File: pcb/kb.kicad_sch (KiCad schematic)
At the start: 131 parts, among them J1 S2B-PH-SM4-TB, SW0 SW_SPDT, SW1 Gateron_LP_2.0, SW10 Gateron_LP_2.0, SW11 Gateron_LP_2.0, SW12 Gateron_LP_2.0, SW13 Gateron_LP_2.0, SW14 Gateron_LP_2.0, SW15 Gateron_LP_2.0, SW16 Gateron_LP_2.0, SW17 Gateron_LP_2.0, SW18 Gateron_LP_2.0, SW19 Gateron_LP_2.0, SW2 Gateron_LP_2.0, SW20 Gateron_LP_2.0, SW21 Gateron_LP_2.0, SW22 Gateron_LP_2.0, SW23 Gateron_LP_2.0, SW24 Gateron_LP_2.0, SW25 Gateron_LP_2.0, SW26 Gateron_LP_2.0, SW27 Gateron_LP_2.0, SW28 Gateron_LP_2.0, SW29 Gateron_LP_2.0, SW3 Gateron_LP_2.0, SW30 Gateron_LP_2.0, SW31 Gateron_LP_2.0, SW32 Gateron_LP_2.0, SW33 Gateron_LP_2.0, SW34 Gateron_LP_2.0, SW35 Gateron_LP_2.0, SW36 Gateron_LP_2.0, SW37 Gateron_LP_2.0, SW38 Gateron_LP_2.0, SW39 Gateron_LP_2.0, SW4 Gateron_LP_2.0, SW40 Gateron_LP_2.0, SW41 Gateron_LP_2.0, SW42 Gateron_LP_2.0, SW43 Gateron_LP_2.0, SW44 Gateron_LP_2.0, SW45 Gateron_LP_2.0, SW46 Gateron_LP_2.0, SW47 Gateron_LP_2.0, SW48 Gateron_LP_2.0, SW49 Gateron_LP_2.0, SW5 Gateron_LP_2.0, SW50 Gateron_LP_2.0, SW51 Gateron_LP_2.0, SW52 Gateron_LP_2.0, SW53 Gateron_LP_2.0, SW54 Gateron_LP_2.0, SW55 Gateron_LP_2.0, SW56 Gateron_LP_2.0, SW57 Gateron_LP_2.0, SW58 Gateron_LP_2.0, SW59 Gateron_LP_2.0, SW6 Gateron_LP_2.0, SW60 Gateron_LP_2.0, SW61 Gateron_LP_2.0, SW62 Gateron_LP_2.0, SW63 Gateron_LP_2.0, SW64 Gateron_LP_2.0, SW7 Gateron_LP_2.0, SW8 Gateron_LP_2.0, SW9 Gateron_LP_2.0, U1 SuperMini nRF52840

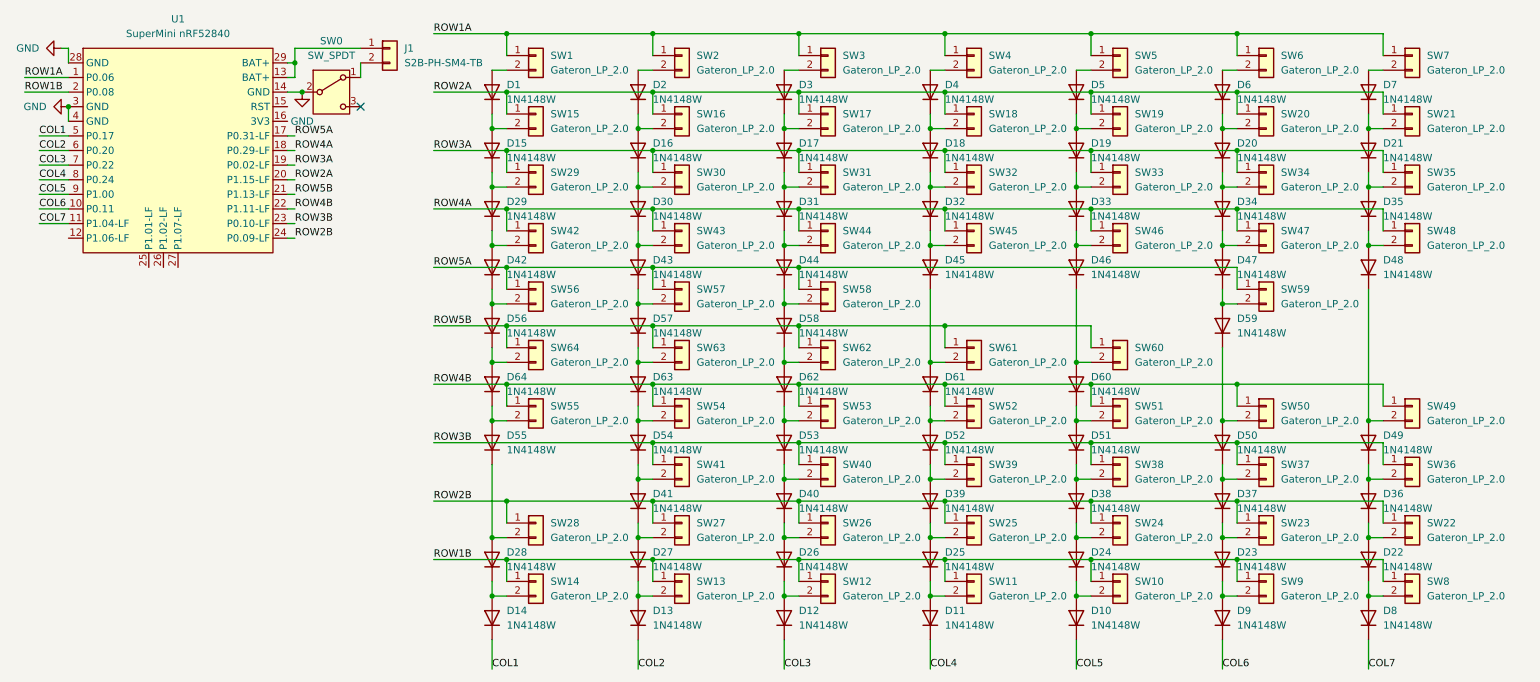
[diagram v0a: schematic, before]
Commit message: parallel diodes
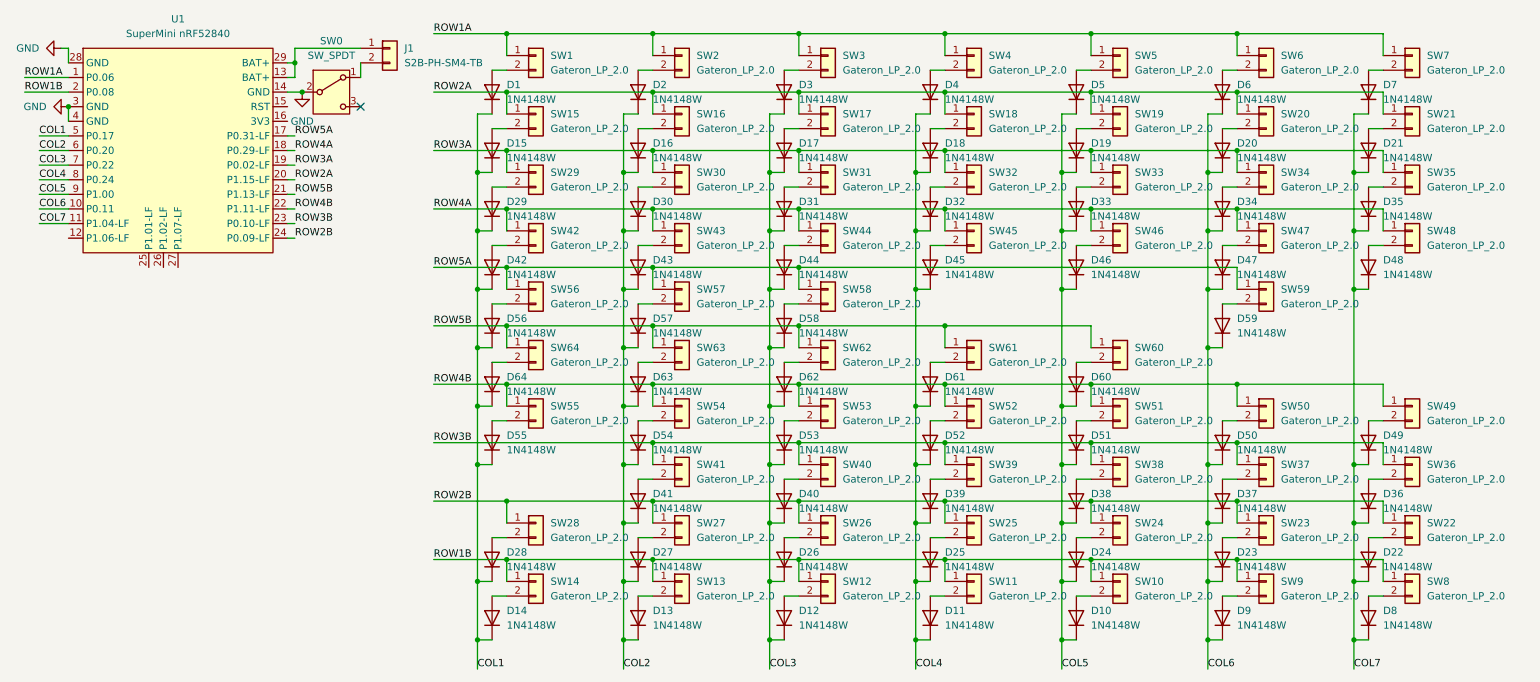
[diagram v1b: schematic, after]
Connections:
- net COL1: now also D1.1 (K), D15.1 (K), D28.1 (K), D29.1 (K), D42.1 (K), D55.1 (K), D56.1 (K), D64.1 (K)
- net COL2: now also D16.1 (K), D2.1 (K), D27.1 (K), D30.1 (K), D41.1 (K), D43.1 (K), D54.1 (K), D57.1 (K), D63.1 (K)
- net COL3: now also D17.1 (K), D26.1 (K), D3.1 (K), D31.1 (K), D40.1 (K), D44.1 (K), D53.1 (K), D58.1 (K), D62.1 (K)
- net COL4: now also D18.1 (K), D25.1 (K), D32.1 (K), D39.1 (K), D4.1 (K), D45.1 (K), D52.1 (K), D61.1 (K)
- net COL5: now also D19.1 (K), D24.1 (K), D33.1 (K), D38.1 (K), D46.1 (K), D5.1 (K), D51.1 (K), D60.1 (K)
- net COL6: now also D20.1 (K), D23.1 (K), D34.1 (K), D37.1 (K), D47.1 (K), D50.1 (K), D59.1 (K), D6.1 (K)
- net COL7: now also D21.1 (K), D22.1 (K), D35.1 (K), D36.1 (K), D48.1 (K), D49.1 (K), D7.1 (K)
- net at D64.2 (A), SW64.2 (Pin_2): no longer D56.1 (K)
- net at D46.2 (A), SW46.2 (Pin_2): no longer D33.1 (K)
- net at D22.2 (A), SW22.2 (Pin_2): no longer D36.1 (K)
- net at D45.2 (A), SW45.2 (Pin_2): no longer D32.1 (K)
- net at D36.2 (A), SW36.2 (Pin_2): no longer D49.1 (K)
- net at D39.2 (A), SW39.2 (Pin_2): no longer D52.1 (K)
- net at D21.2 (A), SW21.2 (Pin_2): no longer D7.1 (K)
- net at D29.2 (A), SW29.2 (Pin_2): no longer D15.1 (K)
- net at D18.2 (A), SW18.2 (Pin_2): no longer D4.1 (K)
- net at D11.2 (A), SW11.2 (Pin_2): no longer D25.1 (K)
- net at D33.2 (A), SW33.2 (Pin_2): no longer D19.1 (K)
- net at D19.2 (A), SW19.2 (Pin_2): no longer D5.1 (K)
- net at D25.2 (A), SW25.2 (Pin_2): no longer D39.1 (K)
- net at D8.2 (A), SW8.2 (Pin_2): no longer D22.1 (K)
- net at D12.2 (A), SW12.2 (Pin_2): no longer D26.1 (K)
- net at D34.2 (A), SW34.2 (Pin_2): no longer D20.1 (K)
- net at D20.2 (A), SW20.2 (Pin_2): no longer D6.1 (K)
- net at D15.2 (A), SW15.2 (Pin_2): no longer D1.1 (K)
- net at D37.2 (A), SW37.2 (Pin_2): no longer D50.1 (K)
- net at D50.2 (A), SW50.2 (Pin_2): no longer D59.1 (K)
- net at D40.2 (A), SW40.2 (Pin_2): no longer D53.1 (K)
- net at D43.2 (A), SW43.2 (Pin_2): no longer D30.1 (K)
- net at D52.2 (A), SW52.2 (Pin_2): no longer D61.1 (K)
- net at D57.2 (A), SW57.2 (Pin_2): no longer D43.1 (K)
- net at D17.2 (A), SW17.2 (Pin_2): no longer D3.1 (K)
- net at D51.2 (A), SW51.2 (Pin_2): no longer D60.1 (K)
- net at D60.2 (A), SW60.2 (Pin_2): no longer D46.1 (K)
- net at D30.2 (A), SW30.2 (Pin_2): no longer D16.1 (K)
- net at D9.2 (A), SW9.2 (Pin_2): no longer D23.1 (K)
- net at D26.2 (A), SW26.2 (Pin_2): no longer D40.1 (K)
- net at D61.2 (A), SW61.2 (Pin_2): no longer D45.1 (K)
- net at D14.2 (A), SW14.2 (Pin_2): no longer D28.1 (K)
- net at D35.2 (A), SW35.2 (Pin_2): no longer D21.1 (K)
- net at D31.2 (A), SW31.2 (Pin_2): no longer D17.1 (K)
- net at D32.2 (A), SW32.2 (Pin_2): no longer D18.1 (K)
- net at D42.2 (A), SW42.2 (Pin_2): no longer D29.1 (K)
- net at D16.2 (A), SW16.2 (Pin_2): no longer D2.1 (K)
- net at D49.2 (A), SW49.2 (Pin_2): no longer D48.1 (K)
- net at D53.2 (A), SW53.2 (Pin_2): no longer D62.1 (K)
- net at D62.2 (A), SW62.2 (Pin_2): no longer D58.1 (K)
- net at D23.2 (A), SW23.2 (Pin_2): no longer D37.1 (K)
- net at D48.2 (A), SW48.2 (Pin_2): no longer D35.1 (K)
- net at D63.2 (A), SW63.2 (Pin_2): no longer D57.1 (K)
- net at D27.2 (A), SW27.2 (Pin_2): no longer D41.1 (K)
- net at D41.2 (A), SW41.2 (Pin_2): no longer D54.1 (K)
- net at D58.2 (A), SW58.2 (Pin_2): no longer D44.1 (K)
- net at D44.2 (A), SW44.2 (Pin_2): no longer D31.1 (K)
- net at D38.2 (A), SW38.2 (Pin_2): no longer D51.1 (K)
- net at D54.2 (A), SW54.2 (Pin_2): no longer D63.1 (K)
- net at D28.2 (A), SW28.2 (Pin_2): no longer D55.1 (K)
- net at D56.2 (A), SW56.2 (Pin_2): no longer D42.1 (K)
- net at D55.2 (A), SW55.2 (Pin_2): no longer D64.1 (K)
- net at D10.2 (A), SW10.2 (Pin_2): no longer D24.1 (K)
- net at D24.2 (A), SW24.2 (Pin_2): no longer D38.1 (K)
- net at D13.2 (A), SW13.2 (Pin_2): no longer D27.1 (K)
- net at D59.2 (A), SW59.2 (Pin_2): no longer D47.1 (K)
- net at D47.2 (A), SW47.2 (Pin_2): no longer D34.1 (K)
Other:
- title: (none) -> KB60

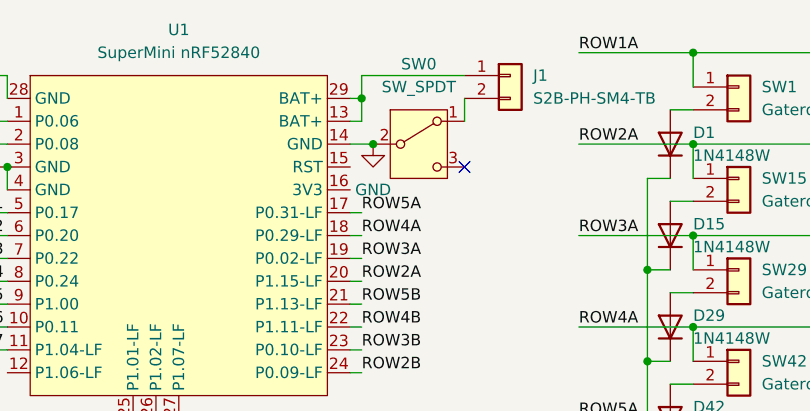
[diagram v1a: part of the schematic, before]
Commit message: fix all known issues with v1.0 pcb
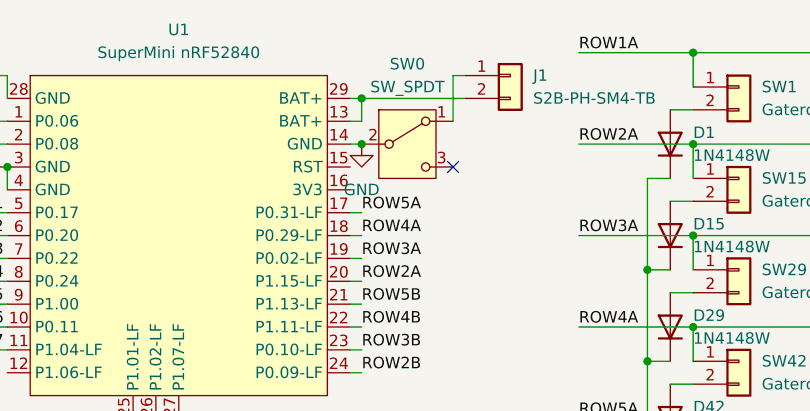
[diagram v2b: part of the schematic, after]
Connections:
- net at U1.13 (BAT+), U1.29 (BAT+): now also J1.2 (Pin_2); no longer J1.1 (Pin_1)
- net at SW0.1 (A): now also J1.1 (Pin_1); no longer J1.2 (Pin_2)
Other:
- moved on the sheet: SW0
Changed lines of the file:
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@@
 	)
 	(junction
+		(at 64.77 26.67)
+		(diameter 0)
+		(color 0 0 0 0)
+	)
+	(junction
 		(at 127 82.55)
 		(diameter 0)
@@
 	)
 	(junction
+		(at 64.77 31.75)
+		(diameter 0)
+		(color 0 0 0 0)
+	)
+	(junction
 		(at 96.52 127)
 		(diameter 0)
@@
 	)
 	(junction
-		(at 66.04 31.75)
-		(diameter 0)
-		(color 0 0 0 0)
-	)
-	(junction
 		(at 177.8 31.75)
 		(diameter 0)
@@
 	)
 	(junction
-		(at 64.77 26.67)
-		(diameter 0)
-		(color 0 0 0 0)
-	)
-	(junction
 		(at 177.8 102.87)
 		(diameter 0)
@@
 	)
 	(no_connect
-		(at 76.2 34.29)
+		(at 74.93 34.29)
 	)
 	(wire
@@
 	(wire
 		(pts
-			(xy 76.2 26.67) (xy 76.2 29.21)
-		)
-		(stroke
-			(width 0)
-			(type default)
-		)
-	)
-	(wire
-		(pts
 			(xy 175.26 119.38) (xy 177.8 119.38)
 		)
@@
 	(wire
 		(pts
+			(xy 74.93 24.13) (xy 74.93 29.21)
+		)
+		(stroke
+			(width 0)
+			(type default)
+		)
+	)
+	(wire
+		(pts
 			(xy 127 52.07) (xy 152.4 52.07)
 		)
@@
 	(wire
 		(pts
+			(xy 64.77 26.67) (xy 76.2 26.67)
+		)
+		(stroke
+			(width 0)
+			(type default)
+		)
+	)
+	(wire
+		(pts
 			(xy 121.92 76.2) (xy 121.92 86.36)
 		)
@@
 	(wire
 		(pts
-			(xy 64.77 24.13) (xy 64.77 26.67)
-		)
-		(stroke
-			(width 0)
-			(type default)
-		)
-	)
-	(wire
-		(pts
 			(xy 96.52 127) (xy 96.52 132.08)
 		)
@@
 	(wire
 		(pts
+			(xy 76.2 24.13) (xy 74.93 24.13)
+		)
+		(stroke
+			(width 0)
+			(type default)
+		)
+	)
+	(wire
+		(pts
 			(xy 175.26 99.06) (xy 177.8 99.06)
 		)
@@
 	(wire
 		(pts
-			(xy 64.77 24.13) (xy 76.2 24.13)
-		)
-		(stroke
-			(width 0)
-			(type default)
-		)
-	)
-	(wire
-		(pts
 			(xy 175.26 88.9) (xy 177.8 88.9)
 		)
@@
 	(wire
 		(pts
-			(xy 63.5 31.75) (xy 66.04 31.75)
+			(xy 63.5 31.75) (xy 64.77 31.75)
 		)
 		(stroke
@@
 	(symbol
 		(lib_id "power:GND")
-		(at 66.04 31.75 0)
+		(at 64.77 31.75 0)
 		(unit 1)
 		(exclude_from_sim no)
@@
 		(fields_autoplaced yes)
 		(property "Reference" "#PWR01"
-			(at 66.04 38.1 0)
+			(at 64.77 38.1 0)
 			(effects
 				(font
@@
 		)
 		(property "Value" "GND"
-			(at 66.04 36.83 0)
+			(at 64.77 36.83 0)
 			(effects
 				(font
@@
 		)
 		(property "Footprint" ""
-			(at 66.04 31.75 0)
+			(at 64.77 31.75 0)
 			(effects
 				(font
@@
 		)
 		(property "Datasheet" ""
-			(at 66.04 31.75 0)
+			(at 64.77 31.75 0)
 			(effects
 				(font
@@
 		)
 		(property "Description" "Power symbol creates a global label with name \"GND\" , ground"
-			(at 66.04 31.75 0)
+			(at 64.77 31.75 0)
 			(effects
 				(font
@@
 	(symbol
 		(lib_id "Switch:SW_SPDT")
-		(at 71.12 31.75 0)
+		(at 69.85 31.75 0)
 		(unit 1)
 		(exclude_from_sim no)
@@
 		(fields_autoplaced yes)
 		(property "Reference" "SW0"
-			(at 71.12 22.86 0)
+			(at 69.85 22.86 0)
 			(effects
 				(font
@@
 		)
 		(property "Value" "SW_SPDT"
-			(at 71.12 25.4 0)
+			(at 69.85 25.4 0)
 			(effects
 				(font
@@
 		)
 		(property "Footprint" "Button_Switch_SMD:SW_SPDT_CK_JS102011SAQN"
-			(at 71.12 31.75 0)
+			(at 69.85 31.75 0)
 			(effects
 				(font
@@
 		)
 		(property "Datasheet" "~"
-			(at 71.12 39.37 0)
+			(at 69.85 39.37 0)
 			(effects
 				(font
@@
 		)
 		(property "Description" "Switch, single pole double throw"
-			(at 71.12 31.75 0)
+			(at 69.85 31.75 0)
 			(effects
 				(font

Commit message: update footprints + bom
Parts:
- SW0: footprint Button_Switch_SMD:SW_SPDT_CK_JS102011SAQN -> alpsalpine:SW_SSSS811101
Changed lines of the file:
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@@
 	(title_block
 		(title "KB60")
-		(date "2025-12-26")
+		(date "2025-12-27")
 		(rev "V1.1")
 	)
@@
 			)
 		)
-		(property "Footprint" "Button_Switch_SMD:SW_SPDT_CK_JS102011SAQN"
+		(property "Footprint" "alpsalpine:SW_SSSS811101"
 			(at 69.85 31.75 0)
 			(effects
